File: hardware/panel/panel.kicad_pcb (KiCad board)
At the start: 2 copper layers, 62 x 104.3 mm, 5 parts

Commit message: Revert "Panel: close mask to the copper edge around the test hole — no FR4 sliver"
This reverts commit eb9a4d2783863aab7f219a44ac207152b572bd98.
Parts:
- moved MT2 100.1 mm to (56.4, 5.64)
- moved MT3 100.1 mm to (5.64, 91.9)
- moved MT1 98.6 mm to (5.64, 5.64)
- moved MT4 98.6 mm to (53.4, 91.9)
- renumbered MT4 to MT1, MT3 to MT2, MT2 to MT3, MT1 to MT4
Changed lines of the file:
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@@
 	(footprint "panel:SMT_Standoff_M2.5_D6.0mm"
 		(layer "B.Cu")
-		(at 5.6364 5.6364)
-		(property "Reference" "MT1"
+		(at 53.3636 91.93)
+		(property "Reference" "MT4"
 			(at 0 0 0)
 			(layer "F.SilkS")
@@
 	(footprint "panel:SMT_Standoff_M2.5_D6.0mm"
 		(layer "B.Cu")
-		(at 53.3636 91.93)
-		(property "Reference" "MT4"
+		(at 5.6364 5.6364)
+		(property "Reference" "MT1"
 			(at 0 0 0)
 			(layer "F.SilkS")
@@
 	(footprint "panel:SMT_Standoff_M2.5_D6.0mm"
 		(layer "B.Cu")
-		(at 56.3636 5.6364)
-		(property "Reference" "MT2"
+		(at 5.6364 91.93)
+		(property "Reference" "MT3"
 			(at 0 0 0)
 			(layer "F.SilkS")
@@
 	(footprint "panel:SMT_Standoff_M2.5_D6.0mm"
 		(layer "B.Cu")
-		(at 5.6364 91.93)
-		(property "Reference" "MT3"
+		(at 56.3636 5.6364)
+		(property "Reference" "MT2"
 			(at 0 0 0)
 			(layer "F.SilkS")
@@
 			(xy 31.925 33.1743) (xy 31.8576 33.4039) (xy 31.8425 33.6833) (xy 31.84527 33.687119) (xy 31.81808 33.696849)
 			(xy 31.765518 33.710015) (xy 31.7522 33.7115) (xy 31.7307 33.714) (xy 31.7167 33.715) (xy 31.6317 33.6951)
-			(xy 31.6088 33.6477) (xy 31.6152 33.5916) (xy 31.6524 33.4174) (xy 31.6896 33.243299) (xy 31.725732 33.0741)
-			(xy 31.739708 33.0691) (xy 31.7888 33.0691) (xy 31.8508 33.0691) (xy 31.9128 33.0691) (xy 31.9201 33.0342)
-			(xy 31.9275 32.9992) (xy 31.929159 32.991264) (xy 32.037072 32.940226) (xy 32.222254 32.829233) (xy 32.395665 32.700622)
-			(xy 32.555634 32.555634) (xy 32.700622 32.395665) (xy 32.829233 32.222254) (xy 32.940226 32.037072)
-			(xy 33.032534 31.841903) (xy 33.105268 31.638626) (xy 33.157727 31.429198) (xy 33.189406 31.215637)
-			(xy 33.2 31) (xy 33.189406 30.784362) (xy 33.157727 30.570801) (xy 33.105268 30.361373) (xy 33.032534 30.158096)
-			(xy 32.940226 29.962927) (xy 32.829233 29.777745) (xy 32.700622 29.604334) (xy 32.555634 29.444365)
-			(xy 32.395665 29.299377) (xy 32.222254 29.170766) (xy 32.037072 29.059773) (xy 31.841903 28.967465)
-			(xy 31.638626 28.894731) (xy 31.429198 28.842272) (xy 31.215637 28.810593) (xy 31 28.8) (xy 30.784362 28.810593)
-			(xy 30.570801 28.842272) (xy 30.361373 28.894731) (xy 30.158096 28.967465) (xy 29.962927 29.059773)
-			(xy 29.777745 29.170766) (xy 29.604334 29.299377) (xy 29.444365 29.444365) (xy 29.299377 29.604334)
-			(xy 29.170766 29.777745) (xy 29.059773 29.962927) (xy 28.967465 30.158096) (xy 28.894731 30.361373)
-			(xy 28.842272 30.570801) (xy 28.810593 30.784362) (xy 28.8 31) (xy 28.810593 31.215637) (xy 28.842272 31.429198)
-			(xy 28.894731 31.638626) (xy 28.967465 31.841903) (xy 29.059773 32.037072) (xy 29.170766 32.222254)
-			(xy 29.299377 32.395665) (xy 29.444365 32.555634) (xy 29.604334 32.700622) (xy 29.777745 32.829233)
-			(xy 29.962927 32.940226) (xy 30.158096 33.032534) (xy 30.361373 33.105268) (xy 30.570801 33.157727)
-			(xy 30.784362 33.189406) (xy 31 33.2) (xy 31.215637 33.189406) (xy 31.429198 33.157727) (xy 31.577276 33.120635)
-			(xy 31.5453 33.2715) (xy 31.5025 33.473799) (xy 31.4596 33.6761) (xy 31.4625 33.7592) (xy 31.478078 33.774688)
-			(xy 31.276231 33.804629) (xy 31 33.8182) (xy 30.723768 33.804629) (xy 30.450196 33.764049) (xy 30.181919 33.696849)
-			(xy 29.921521 33.603677) (xy 29.671509 33.48543) (xy 29.434291 33.343247) (xy 29.212152 33.178498)
-			(xy 29.007231 32.992768) (xy 28.821501 32.787847) (xy 28.656752 32.565708) (xy 28.514569 32.32849)
-			(xy 28.396322 32.078478) (xy 28.30315 31.81808) (xy 28.23595 31.549803) (xy 28.19537 31.276231) (xy 28.1818 31)
-			(xy 28.19537 30.723768) (xy 28.23595 30.450196) (xy 28.30315 30.181919) (xy 28.396322 29.921521)
-			(xy 28.514569 29.671509) (xy 28.656752 29.434291) (xy 28.821501 29.212152) (xy 29.007231 29.007231)
-			(xy 29.212152 28.821501) (xy 29.434291 28.656752) (xy 29.671509 28.514569) (xy 29.921521 28.396322)
-			(xy 30.181919 28.30315) (xy 30.450196 28.23595) (xy 30.723768 28.19537) (xy 31 28.1818)
+			(xy 31.6088 33.6477) (xy 31.6152 33.5916) (xy 31.6524 33.4174) (xy 31.6896 33.243299) (xy 31.7268 33.0691)
+			(xy 31.7888 33.0691) (xy 31.8508 33.0691) (xy 31.9128 33.0691) (xy 31.9201 33.0342) (xy 31.9275 32.9992)
+			(xy 31.9348 32.9643) (xy 31.8728 32.9643) (xy 31.8108 32.9643) (xy 31.7488 32.9643) (xy 31.7651 32.8887)
+			(xy 31.7815 32.8132) (xy 31.797606 32.738595) (xy 31.902724 32.688879) (xy 32.063916 32.592264) (xy 32.214863 32.480315)
+			(xy 32.354109 32.354109) (xy 32.480315 32.214863) (xy 32.592264 32.063916) (xy 32.688879 31.902724)
+			(xy 32.769229 31.732838) (xy 32.83254 31.555895) (xy 32.878203 31.373597) (xy 32.905778 31.187702)
+			(xy 32.915 31) (xy 32.905778 30.812297) (xy 32.878203 30.626402) (xy 32.83254 30.444104) (xy 32.769229 30.267161)
+			(xy 32.688879 30.097275) (xy 32.592264 29.936083) (xy 32.480315 29.785136) (xy 32.354109 29.64589)
+			(xy 32.214863 29.519684) (xy 32.063916 29.407735) (xy 31.902724 29.31112) (xy 31.732838 29.23077)
+			(xy 31.555895 29.167459) (xy 31.373597 29.121796) (xy 31.187702 29.094221) (xy 31 29.085) (xy 30.812297 29.094221)
+			(xy 30.626402 29.121796) (xy 30.444104 29.167459) (xy 30.267161 29.23077) (xy 30.097275 29.31112)
+			(xy 29.936083 29.407735) (xy 29.785136 29.519684) (xy 29.64589 29.64589) (xy 29.519684 29.785136)
+			(xy 29.407735 29.936083) (xy 29.31112 30.097275) (xy 29.23077 30.267161) (xy 29.167459 30.444104)
+			(xy 29.121796 30.626402) (xy 29.094221 30.812297) (xy 29.085 31) (xy 29.094221 31.187702) (xy 29.121796 31.373597)
+			(xy 29.167459 31.555895) (xy 29.23077 31.732838) (xy 29.31112 31.902724) (xy 29.407735 32.063916)
+			(xy 29.519684 32.214863) (xy 29.64589 32.354109) (xy 29.785136 32.480315) (xy 29.936083 32.592264)
+			(xy 30.097275 32.688879) (xy 30.267161 32.769229) (xy 30.444104 32.83254) (xy 30.626402 32.878203)
+			(xy 30.812297 32.905778) (xy 31 32.915) (xy 31.187702 32.905778) (xy 31.373597 32.878203) (xy 31.555895 32.83254)
+			(xy 31.645566 32.800455) (xy 31.6338 32.8549) (xy 31.622 32.909599) (xy 31.6101 32.9643) (xy 31.5634 32.9643)
+			(xy 31.5166 32.9643) (xy 31.4698 32.9643) (xy 31.4625 32.9992) (xy 31.4551 33.0342) (xy 31.4478 33.0691)
+			(xy 31.4946 33.0691) (xy 31.5414 33.0691) (xy 31.5882 33.0691) (xy 31.5453 33.2715) (xy 31.5025 33.473799)
+			(xy 31.4596 33.6761) (xy 31.4625 33.7592) (xy 31.478078 33.774688) (xy 31.276231 33.804629) (xy 31 33.8182)
+			(xy 30.723768 33.804629) (xy 30.450196 33.764049) (xy 30.181919 33.696849) (xy 29.921521 33.603677)
+			(xy 29.671509 33.48543) (xy 29.434291 33.343247) (xy 29.212152 33.178498) (xy 29.007231 32.992768)
+			(xy 28.821501 32.787847) (xy 28.656752 32.565708) (xy 28.514569 32.32849) (xy 28.396322 32.078478)
+			(xy 28.30315 31.81808) (xy 28.23595 31.549803) (xy 28.19537 31.276231) (xy 28.1818 31) (xy 28.19537 30.723768)
+			(xy 28.23595 30.450196) (xy 28.30315 30.181919) (xy 28.396322 29.921521) (xy 28.514569 29.671509)
+			(xy 28.656752 29.434291) (xy 28.821501 29.212152) (xy 29.007231 29.007231) (xy 29.212152 28.821501)
+			(xy 29.434291 28.656752) (xy 29.671509 28.514569) (xy 29.921521 28.396322) (xy 30.181919 28.30315)
+			(xy 30.450196 28.23595) (xy 30.723768 28.19537) (xy 31 28.1818)
 		)
 		(stroke

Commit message: Regenerate fab outputs after the mask-edge revert
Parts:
- moved MT1 98.6 mm to (5.64, 5.64)
- moved MT4 98.6 mm to (53.4, 91.9)
- renumbered MT4 to MT1, MT1 to MT4
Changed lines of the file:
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@@
 	(footprint "panel:SMT_Standoff_M2.5_D6.0mm"
 		(layer "B.Cu")
-		(at 53.3636 91.93)
-		(property "Reference" "MT4"
+		(at 5.6364 5.6364)
+		(property "Reference" "MT1"
 			(at 0 0 0)
 			(layer "F.SilkS")
@@
 	(footprint "panel:SMT_Standoff_M2.5_D6.0mm"
 		(layer "B.Cu")
-		(at 5.6364 5.6364)
-		(property "Reference" "MT1"
+		(at 53.3636 91.93)
+		(property "Reference" "MT4"
 			(at 0 0 0)
 			(layer "F.SilkS")

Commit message: Regenerate panel, combined panel and fab packages
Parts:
- moved MT2 100.1 mm to (56.4, 5.64)
- moved MT3 100.1 mm to (5.64, 91.9)
- renumbered MT3 to MT2, MT2 to MT3
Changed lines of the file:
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@@
 	(footprint "panel:SMT_Standoff_M2.5_D6.0mm"
 		(layer "B.Cu")
-		(at 5.6364 91.93)
-		(property "Reference" "MT3"
+		(at 56.3636 5.6364)
+		(property "Reference" "MT2"
 			(at 0 0 0)
 			(layer "F.SilkS")
@@
 	(footprint "panel:SMT_Standoff_M2.5_D6.0mm"
 		(layer "B.Cu")
-		(at 56.3636 5.6364)
-		(property "Reference" "MT2"
+		(at 5.6364 91.93)
+		(property "Reference" "MT3"
 			(at 0 0 0)
 			(layer "F.SilkS")

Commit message: Pre-order review #2: stitch 10 stranded GND islands, H4 and VBUS via fixes, CAM-clean seam, CTS invert option
Ten top-side GND islands (SP3490, both SP3485 grounds, LED 20 onward, the WROOM's
100 nF caps, CC1's pulldown, SP3232 V+ cap and T2IN tie) had no via to the plane.
KiCad reported them as Zone<->Zone unconnected items and the 08-22 review had
classed those as benign. Twelve vias and three short bottom-side jogs (VBUS trunk
by U1, 3V3 diagonal and VBUS via at H4, DIP5 diagonal by U3) bring the GND net
to one cluster; DRC is 0 errors / 0 unconnected with schematic parity.

Also: second via on the 5 V layer crossing by U1/D10; V-CUT score line and label
moved from Edge.Cuts to User.Comments; H_TEST excluded from pos/BOM; make_fab.sh
regenerates the PCBWay package; firmware gains CONFIG_AIRWRITER_INVERT_CTS and the
serial_out CTS comment now matches the code. Report: docs/review-2026-08-25-pre-order-2.md
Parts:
- moved MT2 100.1 mm to (56.4, 5.64)
- moved MT1 98.6 mm to (5.64, 5.64)
- moved MT4 86.3 mm to (53.4, 91.9)
- moved MT3 86.3 mm to (5.64, 91.9)
- renumbered MT4 to MT1, MT3 to MT2, MT1 to MT3, MT2 to MT4
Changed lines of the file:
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@@
 			)
 		)
+		(attr exclude_from_pos_files exclude_from_bom)
 		(duplicate_pad_numbers_are_jumpers no)
 		(pad "" np_thru_hole circle
@@
 	(footprint "panel:SMT_Standoff_M2.5_D6.0mm"
 		(layer "B.Cu")
+		(at 5.6364 91.93)
+		(property "Reference" "MT3"
+			(at 0 0 0)
+			(layer "F.SilkS")
+			(hide yes)
+			(effects
+				(font
+					(size 1.27 1.27)
+				)
+			)
+		)
+		(property "Value" "9774030151R"
+			(at 0 0 0)
+			(layer "F.Fab")
+			(hide yes)
+			(effects
+				(font
+					(size 1.27 1.27)
+				)
+			)
+		)
+		(property "Datasheet" ""
+			(at 0 0 0)
+			(layer "F.Fab")
+			(hide yes)
+			(effects
+				(font
+					(size 1.27 1.27)
+				)
+			)
+		)
+		(property "Description" ""
+			(at 0 0 0)
+			(layer "F.Fab")
+			(hide yes)
+			(effects
+				(font
+					(size 1.27 1.27)
+				)
+			)
+		)
+		(attr smd)
+		(duplicate_pad_numbers_are_jumpers no)
+		(pad "" smd circle
+			(at 0 0)
+			(size 6 6)
+			(layers "B.Mask")
+		)
+		(embedded_fonts no)
+		(model "${KICAD10_3DMODEL_DIR}/Mounting_Wuerth.3dshapes/Mounting_Wuerth_WA-SMSI-M2.5_H3mm_9774030151.step"
+			(offset
+				(xyz 0 0 0)
+			)
+			(scale
+				(xyz 1 1 1)
+			)
+			(rotate
+				(xyz 0 0 0)
+			)
+		)
+	)
+	(footprint "panel:SMT_Standoff_M2.5_D6.0mm"
+		(layer "B.Cu")
 		(at 5.6364 5.6364)
 		(property "Reference" "MT1"
@@
 			(at 0 0 0)
 			(layer "F.SilkS")
-			(hide yes)
-			(effects
-				(font
-					(size 1.27 1.27)
-				)
-			)
-		)
-		(property "Value" "9774030151R"
-			(at 0 0 0)
-			(layer "F.Fab")
-			(hide yes)
-			(effects
-				(font
-					(size 1.27 1.27)
-				)
-			)
-		)
-		(property "Datasheet" ""
-			(at 0 0 0)
-			(layer "F.Fab")
-			(hide yes)
-			(effects
-				(font
-					(size 1.27 1.27)
-				)
-			)
-		)
-		(property "Description" ""
-			(at 0 0 0)
-			(layer "F.Fab")
-			(hide yes)
-			(effects
-				(font
-					(size 1.27 1.27)
-				)
-			)
-		)
-		(attr smd)
-		(duplicate_pad_numbers_are_jumpers no)
-		(pad "" smd circle
-			(at 0 0)
-			(size 6 6)
-			(layers "B.Mask")
-		)
-		(embedded_fonts no)
-		(model "${KICAD10_3DMODEL_DIR}/Mounting_Wuerth.3dshapes/Mounting_Wuerth_WA-SMSI-M2.5_H3mm_9774030151.step"
-			(offset
-				(xyz 0 0 0)
-			)
-			(scale
-				(xyz 1 1 1)
-			)
-			(rotate
-				(xyz 0 0 0)
-			)
-		)
-	)
-	(footprint "panel:SMT_Standoff_M2.5_D6.0mm"
-		(layer "B.Cu")
-		(at 5.6364 91.93)
-		(property "Reference" "MT3"
-			(at 0 0 0)
-			(layer "F.SilkS")

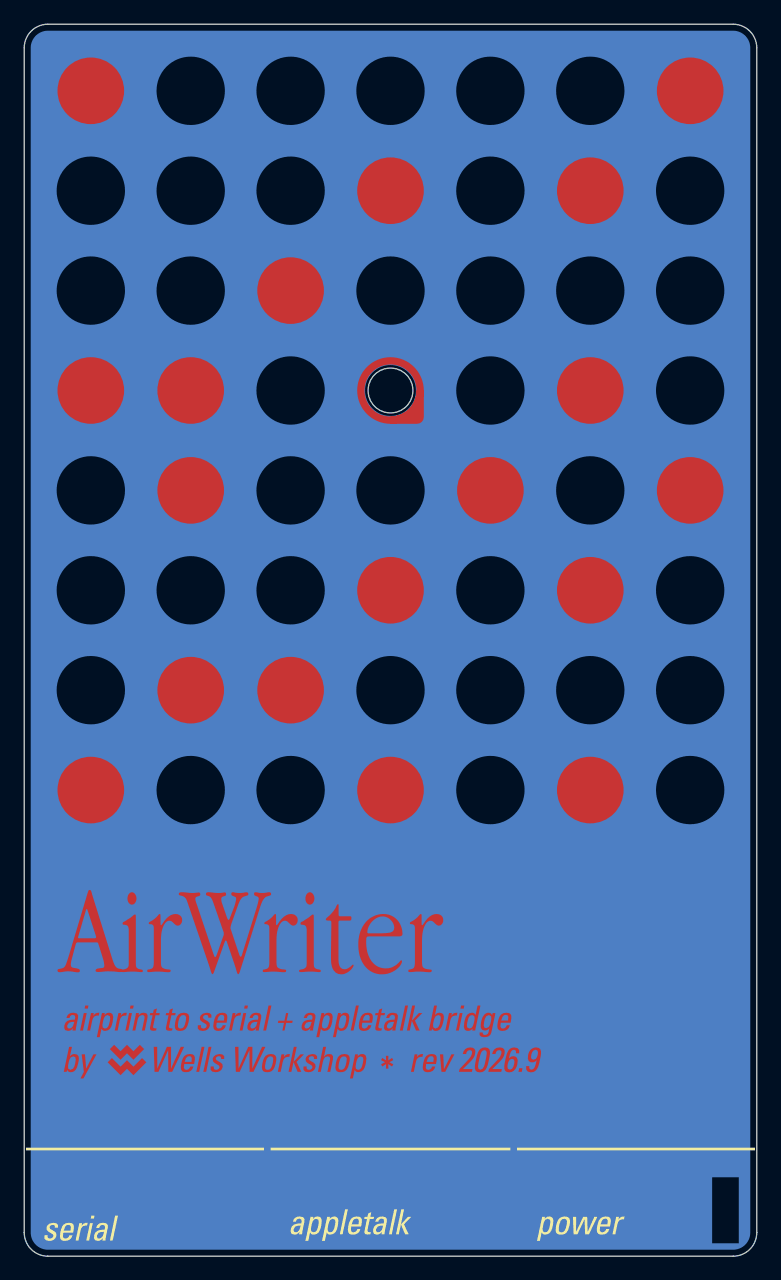
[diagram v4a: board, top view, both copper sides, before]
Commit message: Panel: plate the test hole — gold to the bore, no black surround
The 3.8mm test hole becomes a plated pad (O4.4 pad, copper layers only):
the bore wall takes ENIG and reads gold, the keep_dia black surround and
its sub-0.1mm mask sliver are gone, and mask opens to the drill edge.
Pad + annulus ring + tab art share decorative net PANEL_AU so their
contact doesn't DRC as a short; combine_boards.py carries that one net
through and strips all others (a pad's stripped (net 0) doesn't parse -
delete the node instead). Flood window grown to clear the pad by 0.25mm.
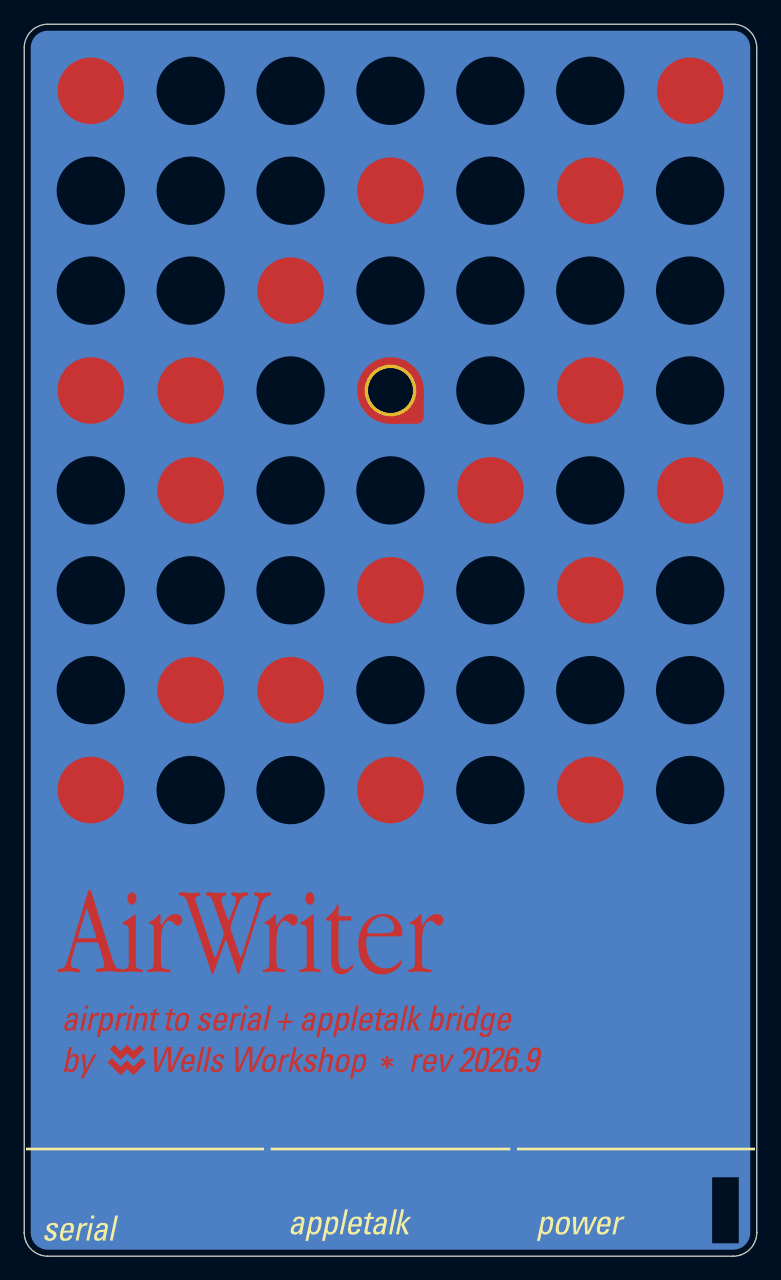
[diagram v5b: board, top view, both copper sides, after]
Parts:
- moved MT3 100.1 mm to (5.64, 91.9)
- moved MT4 98.6 mm to (53.4, 91.9)
- moved MT2 86.3 mm to (56.4, 5.64)
- moved MT1 86.3 mm to (5.64, 5.64)
- renumbered MT3 to MT1, MT4 to MT2, MT2 to MT3, MT1 to MT4
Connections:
- H_TEST pad : (no net) -> PANEL_AU

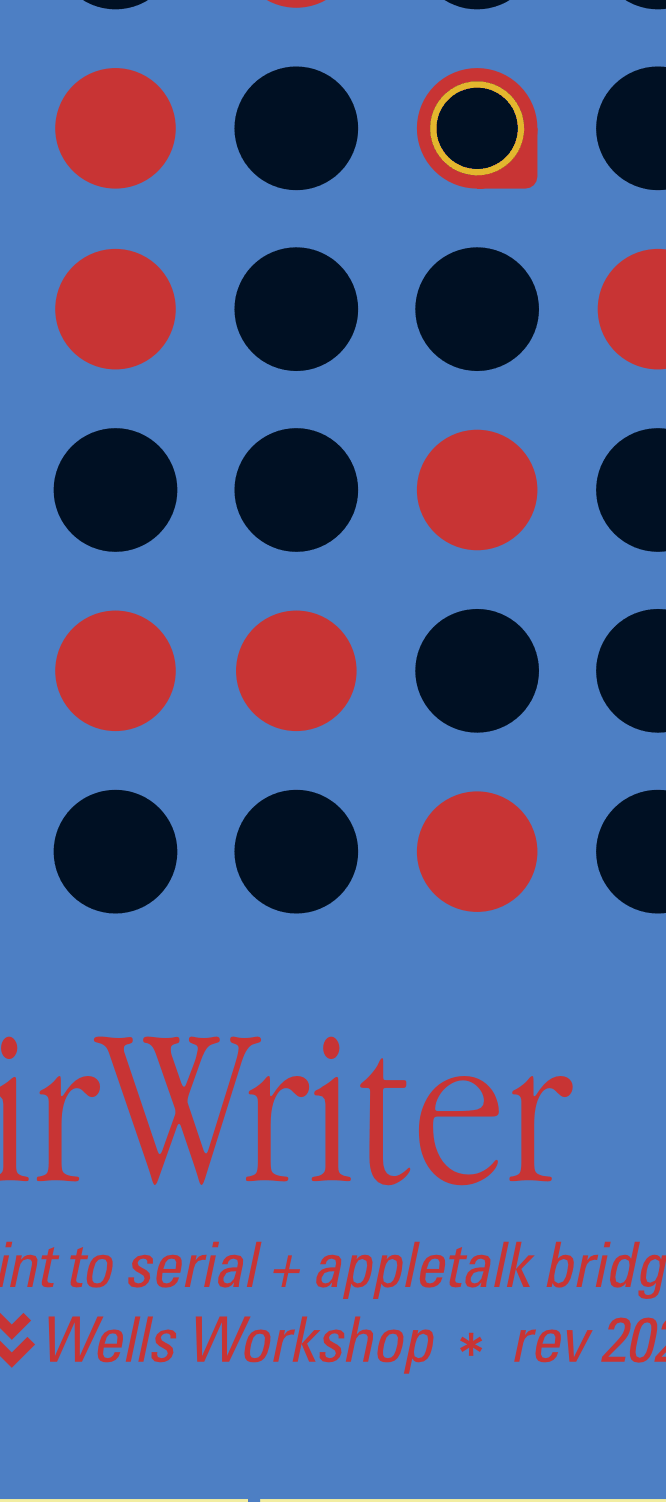
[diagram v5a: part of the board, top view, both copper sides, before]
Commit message: Panel: swap too-small test label for a dot mark (PCBWay EQ)
PCBWay flagged the "test" soldermask label on the cover panel as below
their minimum feature size. Frame 9 drops that four-glyph label and adds a
~0.9mm accent dot in the test cell's lobe, with the lobe corner radius
opened from 10u to 12u.

The dot is emitted as a #111111 mask-knockout path -- the panel pipeline
ignores <circle> and only ingests white/#fff/#111 fills, so a plain black
circle would have been silently dropped. As a knockout it renders as a
kept-soldermask island on exposed gold. Regenerated panel -> combined ->
fab. Smallest B_Mask features in that cell: 0.90mm island, 0.23mm opening.
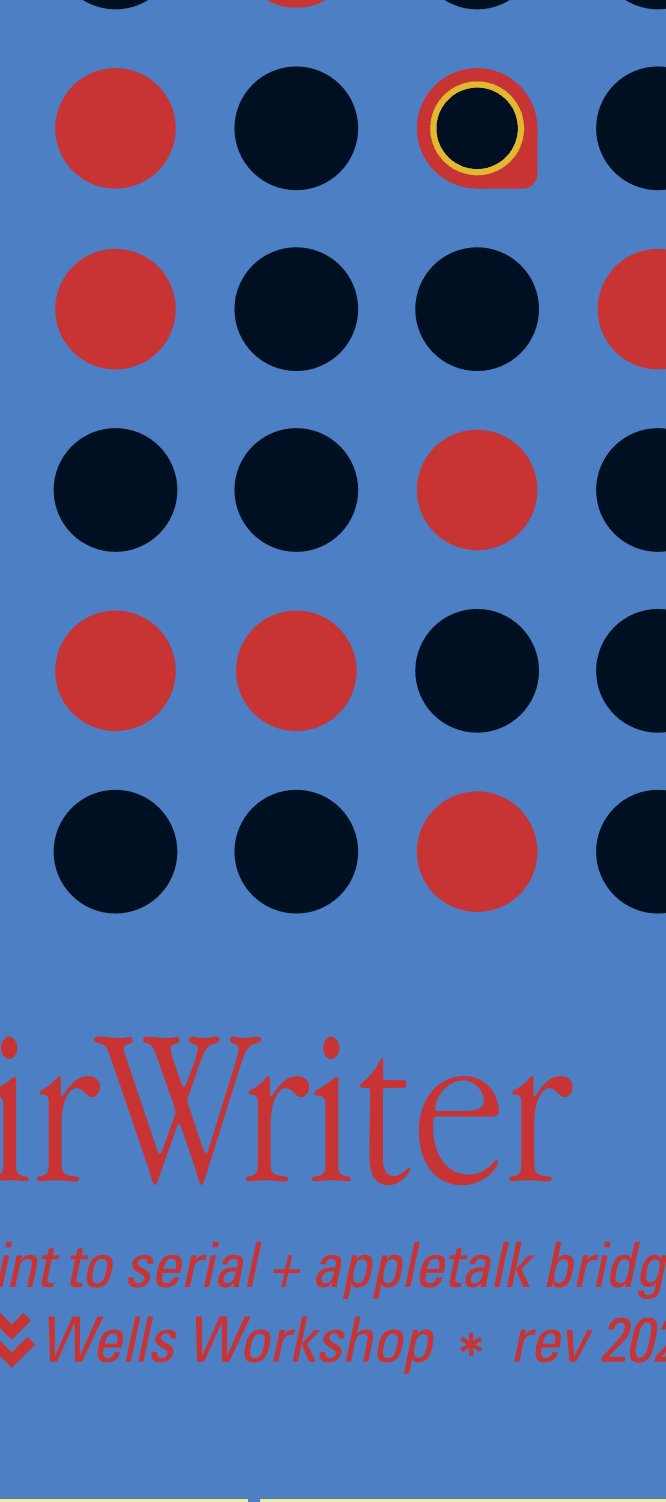
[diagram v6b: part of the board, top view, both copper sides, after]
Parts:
- moved MT2 100.1 mm to (56.4, 5.64)
- moved MT3 100.1 mm to (5.64, 91.9)
- renumbered MT3 to MT2, MT2 to MT3
